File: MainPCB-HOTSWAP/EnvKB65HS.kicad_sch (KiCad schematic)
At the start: 157 parts

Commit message: added i2c header for oled
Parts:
- added J1: Conn_01x04, Connector_PinSocket_2.54mm:PinSocket_1x04_P2.54mm_Vertical, symbol Connector_Generic:Conn_01x04
- D_0, D_1, D_10, D_11, D_12, D_13, D_14, D_15, D_16, D_17, D_18, D_19, D_2, D_20, D_21, D_22, D_23, D_24, D_25, D_26, D_27, D_28, D_29, D_3, D_30, D_31, D_32, D_33, D_34, D_35, D_36, D_37, D_38, D_39, D_4, D_40, D_41, D_42, D_43, D_44, D_45, D_46, D_47, D_48, D_49, D_5, D_50, D_51, D_52, D_53, D_54, D_55, D_56, D_57, D_58, D_59, D_6, D_60, D_61, D_62, D_63, D_64, D_65, D_66, D_67, D_68, D_69, D_7, D_70, D_8, D_9: value (none) -> Diode SOD-323; footprint (none) -> Diode_SMD:D_SOD-323_HandSoldering
- H0, H1, H2, H3, H4, H5: value (none) -> MountingHole; footprint (none) -> MountingHole:MountingHole_2.2mm_M2_Pad_Via
- K_0, K_1, K_10, K_11, K_12, K_13, K_14, K_15, K_16, K_17, K_18, K_19, K_2, K_20, K_21, K_22, K_23, K_24, K_25, K_26, K_27, K_28, K_29, K_3, K_30, K_31, K_32, K_33, K_34, K_35, K_36, K_37, K_38, K_39, K_4, K_40, K_41, K_42, K_43, K_44, K_45, K_46, K_47, K_48, K_49, K_5, K_50, K_51, K_52, K_53, K_54, K_55, K_56, K_57, K_58, K_59, K_6, K_60, K_61, K_62, K_63, K_64, K_65, K_66, K_67, K_68, K_69, K_7, K_70, K_71, K_72, K_8, K_9: value (none) -> KEYSW; footprint (none) -> MX_Only:MXOnly-1U-Hotswap-Modified
- ST1, ST2, ST3, ST4, ST5, ST6: value (none) -> STABILIZER; footprint (none) -> Mounting_Keyboard_Stabilizer:Stabilizer_Cherry_MX_2u
- U0: value (none) -> Pico; footprint (none) -> MCU_RaspberryPi_and_Boards:RPi_Pico_SMD_TH
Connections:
- net GND: now also J1.1 (Pin_1)
- net USBVBUS: now reaches U0.40 (VBUS)
- net USBVBUS: now also J1.2 (Pin_2)
- net GPIO26 renamed I2C-SDA
- net I2C-SDA: now also J1.4 (Pin_4)
- net GPIO27 renamed I2C-SCL
- net I2C-SCL: now also J1.3 (Pin_3)

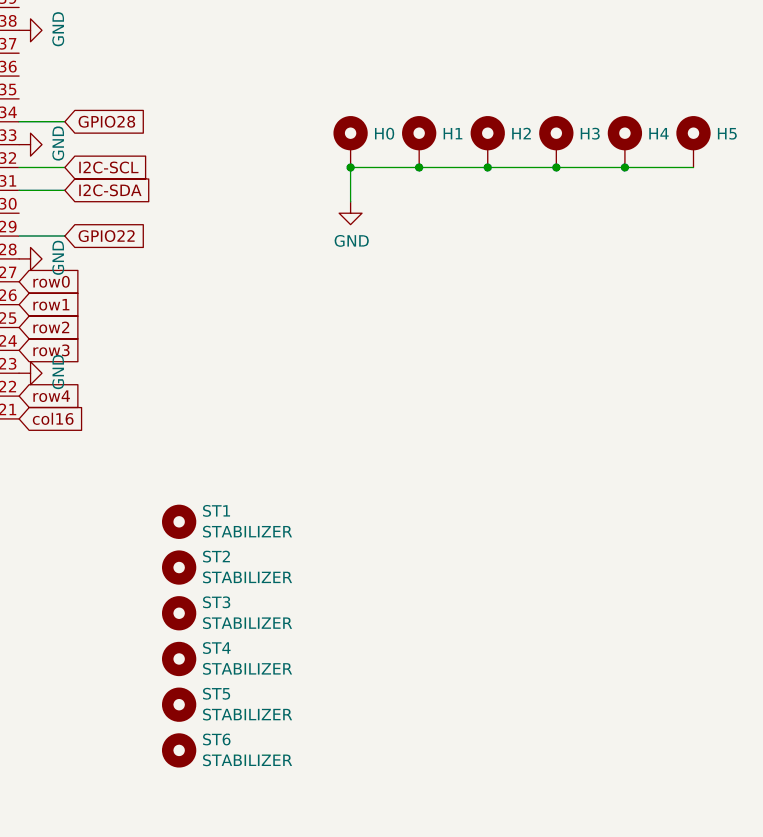
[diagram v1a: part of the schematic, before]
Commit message: swapped mount holes to solderable inserts and fixed some potential clearance issues
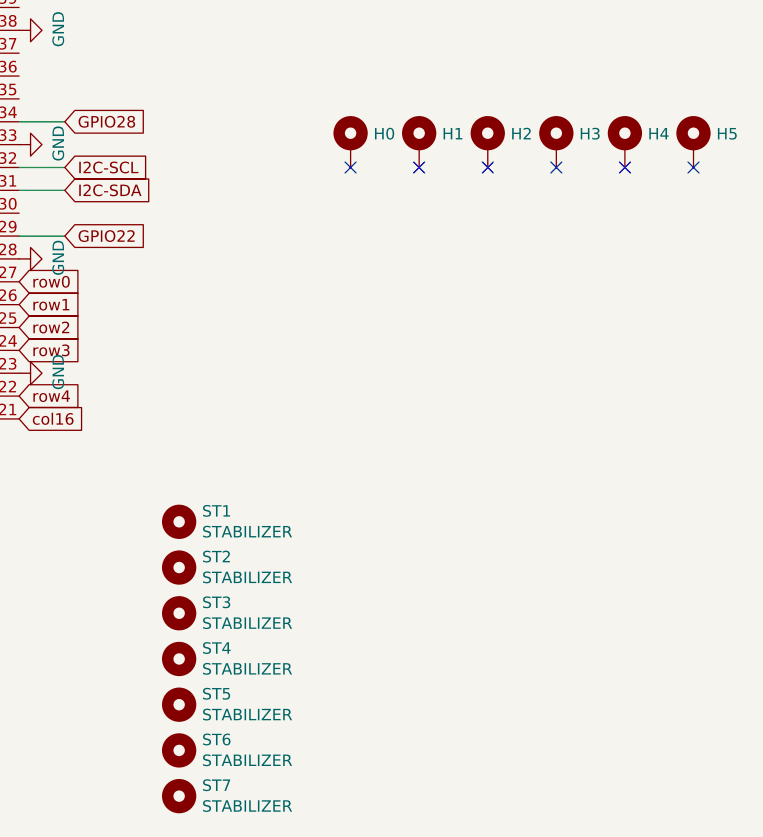
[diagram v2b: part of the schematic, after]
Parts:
- added ST7: STABILIZER, Mounting_Keyboard_Stabilizer:Stabilizer_Cherry_MX_2u, symbol Mechanical:MountingHole
- H0, H1, H2, H3, H4, H5: value MountingHole -> C2928180; footprint MountingHole:MountingHole_2.2mm_M2_Pad_Via -> Logo:MountingHole_3mm_Pad5.3mm
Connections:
- net GND: no longer H0.1, H1.1, H2.1, H3.1, H4.1, H5.1
- no-connect marks 0 -> 6
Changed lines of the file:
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@@
   (junction (at 212.09 111.76) (diameter 0) (color 0 0 0 0)
   )
-  (junction (at 549.91 73.66) (diameter 0) (color 0 0 0 0)
-  )
   (junction (at 198.12 100.33) (diameter 0) (color 0 0 0 0)
   )
@@
   (junction (at 45.72 100.33) (diameter 0) (color 0 0 0 0)
   )
-  (junction (at 557.53 73.66) (diameter 0) (color 0 0 0 0)
-  )
   (junction (at 364.49 137.16) (diameter 0) (color 0 0 0 0)
   )
@@
   (junction (at 325.12 24.13) (diameter 0) (color 0 0 0 0)
   )
-  (junction (at 572.77 73.66) (diameter 0) (color 0 0 0 0)
-  )
   (junction (at 186.69 86.36) (diameter 0) (color 0 0 0 0)
   )
@@
   (junction (at 389.89 137.16) (diameter 0) (color 0 0 0 0)
   )
-  (junction (at 542.29 73.66) (diameter 0) (color 0 0 0 0)
-  )
   (junction (at 401.32 74.93) (diameter 0) (color 0 0 0 0)
   )
@@
   (junction (at 394.97 74.93) (diameter 0) (color 0 0 0 0)
   )
-  (junction (at 565.15 73.66) (diameter 0) (color 0 0 0 0)
-  )
+  (no_connect (at 542.29 73.66))
+  (no_connect (at 549.91 73.66))
+  (no_connect (at 557.53 73.66))
+  (no_connect (at 565.15 73.66))
+  (no_connect (at 572.77 73.66))
+  (no_connect (at 580.39 73.66))
   (wire (pts (xy 110.49 35.56) (xy 135.89 35.56))
     (stroke (width 0) (type default) (color 0 0 0 0))
@@
     (stroke (width 0) (type default) (color 0 0 0 0))
   )
-  (wire (pts (xy 580.39 73.66) (xy 572.77 73.66))
-    (stroke (width 0) (type default) (color 0 0 0 0))
-  )
   (wire (pts (xy 313.69 80.01) (xy 313.69 81.28))
     (stroke (width 0) (type default) (color 0 0 0 0))
@@
     (stroke (width 0) (type default) (color 0 0 0 0))
   )
-  (wire (pts (xy 572.77 73.66) (xy 565.15 73.66))
-    (stroke (width 0) (type default) (color 0 0 0 0))
-  )
   (wire (pts (xy 198.12 125.73) (xy 198.12 100.33))
     (stroke (width 0) (type default) (color 0 0 0 0))
@@
     (stroke (width 0) (type default) (color 0 0 0 0))
   )
-  (wire (pts (xy 542.29 73.66) (xy 542.29 77.47))
-    (stroke (width 0) (type default) (color 0 0 0 0))
-  )
   (wire (pts (xy 364.49 60.96) (xy 389.89 60.96))
     (stroke (width 0) (type default) (color 0 0 0 0))
@@
     (stroke (width 0) (type default) (color 0 0 0 0))
   )
-  (wire (pts (xy 549.91 73.66) (xy 542.29 73.66))
-    (stroke (width 0) (type default) (color 0 0 0 0))
-  )
   (wire (pts (xy 71.12 24.13) (xy 71.12 100.33))
     (stroke (width 0) (type default) (color 0 0 0 0))
@@
     (stroke (width 0) (type default) (color 0 0 0 0))
   )
-  (wire (pts (xy 557.53 73.66) (xy 549.91 73.66))
-    (stroke (width 0) (type default) (color 0 0 0 0))
-  )
-  (wire (pts (xy 565.15 73.66) (xy 557.53 73.66))
-    (stroke (width 0) (type default) (color 0 0 0 0))
-  )
   (wire (pts (xy 242.57 74.93) (xy 248.92 74.93))
     (stroke (width 0) (type default) (color 0 0 0 0))
@@
       (effects (font (size 1.27 1.27)) (justify left))
     )
-    (property "Value" "MountingHole" (id 1) (at 544.83 72.263 0)
+    (property "Value" "C2928180" (id 1) (at 544.83 72.263 0)
       (effects (font (size 1.27 1.27)) (justify left) hide)
     )
-    (property "Footprint" "MountingHole:MountingHole_2.2mm_M2_Pad_Via" (id 2) (at 542.29 71.12 0)
+    (property "Footprint" "Logo:MountingHole_3mm_Pad5.3mm" (id 2) (at 542.29 71.12 0)
       (effects (font (size 1.27 1.27)) hide)
     )
@@
       (effects (font (size 1.27 1.27)) (justify left))
     )
-    (property "Value" "MountingHole" (id 1) (at 552.45 72.263 0)
+    (property "Value" "C2928180" (id 1) (at 552.45 72.263 0)
       (effects (font (size 1.27 1.27)) (justify left) hide)
     )
-    (property "Footprint" "MountingHole:MountingHole_2.2mm_M2_Pad_Via" (id 2) (at 549.91 71.12 0)
+    (property "Footprint" "Logo:MountingHole_3mm_Pad5.3mm" (id 2) (at 549.91 71.12 0)
       (effects (font (size 1.27 1.27)) hide)
     )
@@
       (effects (font (size 1.27 1.27)) (justify left))
     )
-    (property "Value" "MountingHole" (id 1) (at 560.07 72.263 0)
+    (property "Value" "C2928180" (id 1) (at 560.07 72.263 0)
       (effects (font (size 1.27 1.27)) (justify left) hide)
     )
-    (property "Footprint" "MountingHole:MountingHole_2.2mm_M2_Pad_Via" (id 2) (at 557.53 71.12 0)
+    (property "Footprint" "Logo:MountingHole_3mm_Pad5.3mm" (id 2) (at 557.53 71.12 0)
       (effects (font (size 1.27 1.27)) hide)
     )
@@
       (effects (font (size 1.27 1.27)) (justify left))
     )
-    (property "Value" "MountingHole" (id 1) (at 567.69 72.263 0)
+    (property "Value" "C2928180" (id 1) (at 567.69 72.263 0)
       (effects (font (size 1.27 1.27)) (justify left) hide)
     )
-    (property "Footprint" "MountingHole:MountingHole_2.2mm_M2_Pad_Via" (id 2) (at 565.15 71.12 0)
+    (property "Footprint" "Logo:MountingHole_3mm_Pad5.3mm" (id 2) (at 565.15 71.12 0)
       (effects (font (size 1.27 1.27)) hide)
     )
@@
       (effects (font (size 1.27 1.27)) (justify left))
     )
-    (property "Value" "MountingHole" (id 1) (at 575.31 72.263 0)
+    (property "Value" "C2928180" (id 1) (at 575.31 72.263 0)
       (effects (font (size 1.27 1.27)) (justify left) hide)
     )
-    (property "Footprint" "MountingHole:MountingHole_2.2mm_M2_Pad_Via" (id 2) (at 572.77 71.12 0)
+    (property "Footprint" "Logo:MountingHole_3mm_Pad5.3mm" (id 2) (at 572.77 71.12 0)
       (effects (font (size 1.27 1.27)) hide)
     )
@@
       (effects (font (size 1.27 1.27)) (justify left))
     )
-    (property "Value" "MountingHole" (id 1) (at 582.93 72.263 0)
+    (property "Value" "C2928180" (id 1) (at 582.93 72.263 0)
       (effects (font (size 1.27 1.27)) (justify left) hide)
     )
-    (property "Footprint" "MountingHole:MountingHole_2.2mm_M2_Pad_Via" (id 2) (at 580.39 71.12 0)
+    (property "Footprint" "Logo:MountingHole_3mm_Pad5.3mm" (id 2) (at 580.39 71.12 0)
       (effects (font (size 1.27 1.27)) hide)
     )
@@
     )
   )
-  (symbol (lib_id "power:GND") (at 542.29 77.47 0) (unit 1)
-    (in_bom yes) (on_board yes)
-    (property "Reference" "#PWR0101" (id 0) (at 542.29 83.82 0)
-      (effects (font (size 1.27 1.27)) hide)
-    )
-    (property "Value" "GND" (id 1) (at 542.417 81.8642 0))
-    (property "Footprint" "" (id 2) (at 542.29 77.47 0)
-      (effects (font (size 1.27 1.27)) hide)
-    )
-    (property "Datasheet" "" (id 3) (at 542.29 77.47 0)
-      (effects (font (size 1.27 1.27)) hide)
-    )
-    (pin "1")
-  )
   (symbol (lib_id "power:GND") (at 505.46 96.52 90) (unit 1)
     (in_bom yes) (on_board yes)
@@
     (pin "1")
   )
+  (symbol (lib_id "Mechanical:MountingHole") (at 523.24 143.51 0) (unit 1)
+    (in_bom yes) (on_board yes)
+    (property "Reference" "ST7" (id 0) (at 525.78 142.3416 0)
+      (effects (font (size 1.27 1.27)) (justify left))
+    )
+    (property "Value" "STABILIZER" (id 1) (at 525.78 144.653 0)
+      (effects (font (size 1.27 1.27)) (justify left))
+    )
+    (property "Footprint" "Mounting_Keyboard_Stabilizer:Stabilizer_Cherry_MX_2u" (id 2) (at 523.24 143.51 0)
+      (effects (font (size 1.27 1.27)) hide)
+    )
+    (property "Datasheet" "~" (id 3) (at 523.24 143.51 0)
+      (effects (font (size 1.27 1.27)) hide)
+    )
+  )
   (symbol (lib_id "Device:D_Small") (at 34.29 33.02 90) (unit 1)
     (in_bom yes) (on_board yes)
@@
   )
   (symbol_instances
-    (path "/00000000-0000-0000-0000-000061b0431c"
-      (reference "#PWR0101") (unit 1) (value "GND") (footprint "")
-    )
     (path "/00000000-0000-0000-0000-000061b236da"
       (reference "#PWR0102") (unit 1) (value "GND") (footprint "")
@@
     )
     (path "/00000000-0000-0000-0000-000060ac66fb"
-      (reference "H0") (unit 1) (value "MountingHole") (footprint "MountingHole:MountingHole_2.2mm_M2_Pad_Via")
+      (reference "H0") (unit 1) (value "C2928180") (footprint "Logo:MountingHole_3mm_Pad5.3mm")
     )
     (path "/00000000-0000-0000-0000-000060acbe92"
-      (reference "H1") (unit 1) (value "MountingHole") (footprint "MountingHole:MountingHole_2.2mm_M2_Pad_Via")
+      (reference "H1") (unit 1) (value "C2928180") (footprint "Logo:MountingHole_3mm_Pad5.3mm")
     )
     (path "/00000000-0000-0000-0000-000060ae412b"
-      (reference "H2") (unit 1) (value "MountingHole") (footprint "MountingHole:MountingHole_2.2mm_M2_Pad_Via")
+      (reference "H2") (unit 1) (value "C2928180") (footprint "Logo:MountingHole_3mm_Pad5.3mm")
     )
     (path "/00000000-0000-0000-0000-000060afc1c3"
-      (reference "H3") (unit 1) (value "MountingHole") (footprint "MountingHole:MountingHole_2.2mm_M2_Pad_Via")
+      (reference "H3") (unit 1) (value "C2928180") (footprint "Logo:MountingHole_3mm_Pad5.3mm")
     )
     (path "/00000000-0000-0000-0000-000060b142b5"
-      (reference "H4") (unit 1) (value "MountingHole") (footprint "MountingHole:MountingHole_2.2mm_M2_Pad_Via")
+      (reference "H4") (unit 1) (value "C2928180") (footprint "Logo:MountingHole_3mm_Pad5.3mm")
     )
     (path "/00000000-0000-0000-0000-000060b2c4b8"
-      (reference "H5") (unit 1) (value "MountingHole") (footprint "MountingHole:MountingHole_2.2mm_M2_Pad_Via")
+      (reference "H5") (unit 1) (value "C2928180") (footprint "Logo:MountingHole_3mm_Pad5.3mm")
     )
     (path "/71e681d9-af3d-408d-a1f2-12eb69afec3c"
@@
       (reference "ST6") (unit 1) (value "STABILIZER") (footprint "Mounting_Keyboard_Stabilizer:Stabilizer_Cherry_MX_2u")
     )
+    (path "/b0eb4214-7a24-41d3-a6da-caf5f7eb6626"
+      (reference "ST7") (unit 1) (value "STABILIZER") (footprint "Mounting_Keyboard_Stabilizer:Stabilizer_Cherry_MX_2u")
+    )
     (path "/00000000-0000-0000-0000-000060b33d1a"

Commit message: swapped mount holes back and generated updated gerbers and etc
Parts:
- H0, H1, H2, H3, H4, H5: footprint Logo:MountingHole_3mm_Pad5.3mm -> MountingHole:MountingHole_3.5mm
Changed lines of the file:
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@@
       (effects (font (size 1.27 1.27)) (justify left) hide)
     )
-    (property "Footprint" "Logo:MountingHole_3mm_Pad5.3mm" (id 2) (at 542.29 71.12 0)
+    (property "Footprint" "MountingHole:MountingHole_3.5mm" (id 2) (at 542.29 71.12 0)
       (effects (font (size 1.27 1.27)) hide)
     )
@@
       (effects (font (size 1.27 1.27)) (justify left) hide)
     )
-    (property "Footprint" "Logo:MountingHole_3mm_Pad5.3mm" (id 2) (at 549.91 71.12 0)
+    (property "Footprint" "MountingHole:MountingHole_3.5mm" (id 2) (at 549.91 71.12 0)
       (effects (font (size 1.27 1.27)) hide)
     )
@@
       (effects (font (size 1.27 1.27)) (justify left) hide)
     )
-    (property "Footprint" "Logo:MountingHole_3mm_Pad5.3mm" (id 2) (at 557.53 71.12 0)
+    (property "Footprint" "MountingHole:MountingHole_3.5mm" (id 2) (at 557.53 71.12 0)
       (effects (font (size 1.27 1.27)) hide)
     )
@@
       (effects (font (size 1.27 1.27)) (justify left) hide)
     )
-    (property "Footprint" "Logo:MountingHole_3mm_Pad5.3mm" (id 2) (at 565.15 71.12 0)
+    (property "Footprint" "MountingHole:MountingHole_3.5mm" (id 2) (at 565.15 71.12 0)
       (effects (font (size 1.27 1.27)) hide)
     )
@@
       (effects (font (size 1.27 1.27)) (justify left) hide)
     )
-    (property "Footprint" "Logo:MountingHole_3mm_Pad5.3mm" (id 2) (at 572.77 71.12 0)
+    (property "Footprint" "MountingHole:MountingHole_3.5mm" (id 2) (at 572.77 71.12 0)
       (effects (font (size 1.27 1.27)) hide)
     )
@@
       (effects (font (size 1.27 1.27)) (justify left) hide)
     )
-    (property "Footprint" "Logo:MountingHole_3mm_Pad5.3mm" (id 2) (at 580.39 71.12 0)
+    (property "Footprint" "MountingHole:MountingHole_3.5mm" (id 2) (at 580.39 71.12 0)
       (effects (font (size 1.27 1.27)) hide)
     )
@@
     )
     (path "/00000000-0000-0000-0000-000060ac66fb"
-      (reference "H0") (unit 1) (value "C2928180") (footprint "Logo:MountingHole_3mm_Pad5.3mm")
+      (reference "H0") (unit 1) (value "C2928180") (footprint "MountingHole:MountingHole_3.5mm")
     )
     (path "/00000000-0000-0000-0000-000060acbe92"
-      (reference "H1") (unit 1) (value "C2928180") (footprint "Logo:MountingHole_3mm_Pad5.3mm")
+      (reference "H1") (unit 1) (value "C2928180") (footprint "MountingHole:MountingHole_3.5mm")
     )
     (path "/00000000-0000-0000-0000-000060ae412b"
-      (reference "H2") (unit 1) (value "C2928180") (footprint "Logo:MountingHole_3mm_Pad5.3mm")
+      (reference "H2") (unit 1) (value "C2928180") (footprint "MountingHole:MountingHole_3.5mm")
     )
     (path "/00000000-0000-0000-0000-000060afc1c3"
-      (reference "H3") (unit 1) (value "C2928180") (footprint "Logo:MountingHole_3mm_Pad5.3mm")
+      (reference "H3") (unit 1) (value "C2928180") (footprint "MountingHole:MountingHole_3.5mm")
     )
     (path "/00000000-0000-0000-0000-000060b142b5"
-      (reference "H4") (unit 1) (value "C2928180") (footprint "Logo:MountingHole_3mm_Pad5.3mm")
+      (reference "H4") (unit 1) (value "C2928180") (footprint "MountingHole:MountingHole_3.5mm")
     )
     (path "/00000000-0000-0000-0000-000060b2c4b8"
-      (reference "H5") (unit 1) (value "C2928180") (footprint "Logo:MountingHole_3mm_Pad5.3mm")
+      (reference "H5") (unit 1) (value "C2928180") (footprint "MountingHole:MountingHole_3.5mm")
     )
     (path "/71e681d9-af3d-408d-a1f2-12eb69afec3c"

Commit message: swapped diodes to larger footprint and corrected DRC errors
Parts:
- D_0, D_1, D_10, D_11, D_12, D_13, D_14, D_15, D_16, D_17, D_18, D_19, D_2, D_20, D_21, D_22, D_23, D_24, D_25, D_26, D_27, D_28, D_29, D_3, D_30, D_31, D_32, D_33, D_34, D_35, D_36, D_37, D_38, D_39, D_4, D_40, D_41, D_42, D_43, D_44, D_45, D_46, D_47, D_48, D_49, D_5, D_50, D_51, D_52, D_53, D_54, D_55, D_56, D_57, D_58, D_59, D_6, D_60, D_61, D_62, D_63, D_64, D_65, D_66, D_67, D_68, D_69, D_7, D_70, D_8, D_9: value Diode SOD-323 -> 1n4148; footprint Diode_SMD:D_SOD-323_HandSoldering -> Diode_SMD:D_SOD-123
